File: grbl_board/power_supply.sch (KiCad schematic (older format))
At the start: 26 parts, among them J5 Screw_Terminal_01x04, U3 LT1962-5, U4 BD9G341EFJ

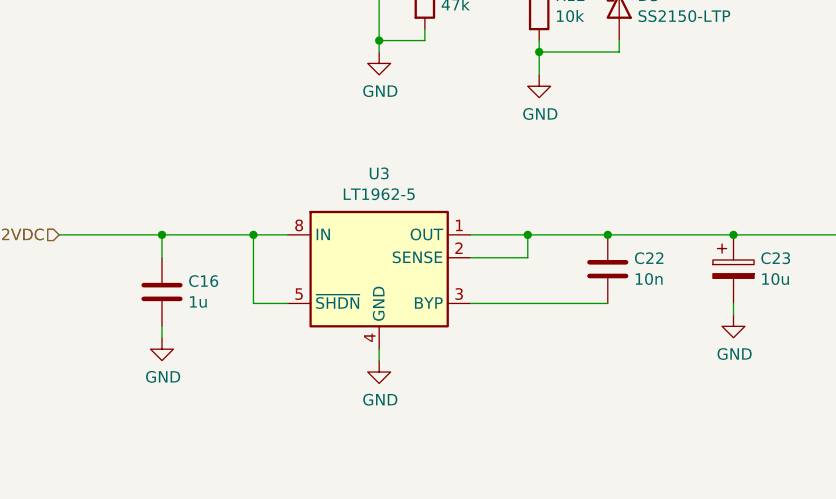
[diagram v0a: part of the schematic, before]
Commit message: fixed pullup resistors on board, and 5v regulator overheating, and stepper driver flipped
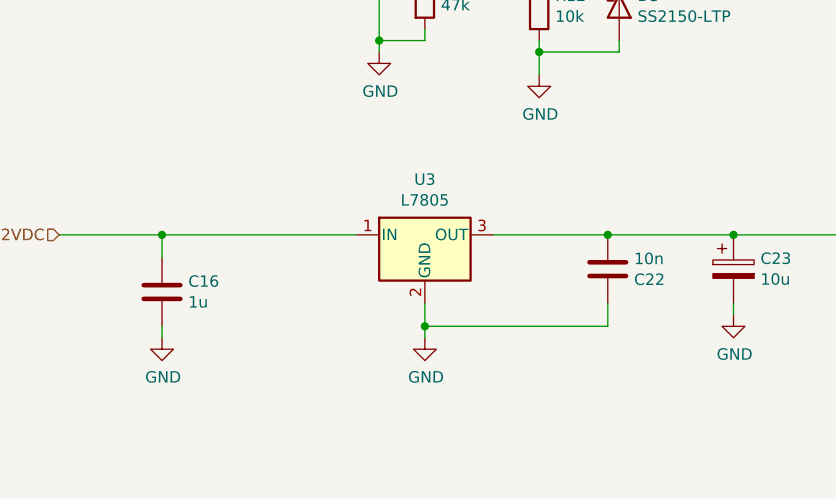
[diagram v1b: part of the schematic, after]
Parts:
- removed U3: LT1962-5, Package_SO:MSOP-8_3x3mm_P0.65mm, symbol Regulator_Linear:LT1962-5
- added U3: L7805, Package_TO_SOT_SMD:TO-263-2, symbol Regulator_Linear:L7805
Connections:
- net 12VDC: now also U3.1 (IN)
- net GND: now also C22.1, U3.2 (GND)
- net at C23.1, F2.2: now also C22.2, U3.3 (OUT); no longer C22.1
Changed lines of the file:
@@
 Text HLabel 7600 2800 2    50   Input ~ 0
 12VDC
-$Comp
-L Regulator_Linear:LT1962-5 U3
-U 1 1 617DD5A8
-P 5100 5050
-F 0 "U3" H 5100 5517 50  0000 C CNN
-F 1 "LT1962-5" H 5100 5426 50  0000 C CNN
-F 2 "Package_SO:MSOP-8_3x3mm_P0.65mm" H 5100 4700 50  0001 C CNN
-F 3 "https://www.analog.com/media/en/technical-documentation/data-sheets/1962fb.pdf" H 5100 4500 50  0001 C CNN
-F 4 "LT1962EMS8-5#TRPBFCT-ND" H 5100 5050 50  0001 C CNN "Digikey Part No."
-	1    5100 5050
-	1    0    0    -1
-$EndComp
 Text HLabel 3700 4850 0    50   Input ~ 0
 12VDC
 Wire Wire Line
 	3700 4850 4150 4850
-Wire Wire Line
-	4550 4850 4550 5150
-Wire Wire Line
-	4550 5150 4700 5150
-Connection ~ 4550 4850
-Wire Wire Line
-	4550 4850 4700 4850
 $Comp
 L Device:C C16
@@
 Wire Wire Line
 	4150 4950 4150 4850
-Connection ~ 4150 4850
-Wire Wire Line
-	4150 4850 4550 4850
 $Comp
 L power:GND #PWR022
@@
 	1    0    0    -1
 $EndComp
-$Comp
-L power:GND #PWR025
-U 1 1 617E1EFF
-P 5100 5400
-F 0 "#PWR025" H 5100 5150 50  0001 C CNN
-F 1 "GND" H 5105 5227 50  0000 C CNN
-F 2 "" H 5100 5400 50  0001 C CNN
-F 3 "" H 5100 5400 50  0001 C CNN
-	1    5100 5400
-	1    0    0    -1
-$EndComp
-Wire Wire Line
-	5100 5400 5100 5350
 Wire Wire Line
 	4150 5300 4150 5250
@@
 F 4 "1276-1009-1-ND" H 6100 5000 50  0001 C CNN "Digikey Part No."
 	1    6100 5000
-	1    0    0    -1
-$EndComp
-Wire Wire Line
-	6100 5150 5500 5150
-Wire Wire Line
-	6100 4850 5750 4850
-Wire Wire Line
-	5500 4950 5750 4950
-Wire Wire Line
-	5750 4950 5750 4850
-Connection ~ 5750 4850
-Wire Wire Line
-	5750 4850 5500 4850
+	1    0    0    1
+$EndComp
 $Comp
 L power:GND #PWR028
@@
 Wire Wire Line
 	6100 4850 6650 4850
-Connection ~ 6100 4850
 Connection ~ 6650 4850
 $Comp
@@
 	3800 1750 3700 1750
 Connection ~ 3800 1750
+$Comp
+L Regulator_Linear:L7805 U?
+U 1 1 61B77D83
+P 5300 4850
+AR Path="/61DA711F/61B77D83" Ref="U?"  Part="1"
+AR Path="/619755E7/61B77D83" Ref="U3"  Part="1"
+F 0 "U3" H 5300 5092 50  0000 C CNN
+F 1 "L7805" H 5300 5001 50  0000 C CNN
+F 2 "Package_TO_SOT_SMD:TO-263-2" H 5325 4700 50  0001 L CIN
+F 3 "http://www.st.com/content/ccc/resource/technical/document/datasheet/41/4f/b3/b0/12/d4/47/88/CD00000444.pdf/files/CD00000444.pdf/jcr:content/translations/en.CD00000444.pdf" H 5300 4800 50  0001 C CNN
+F 4 "497-1170-1-ND" H 5300 4850 50  0001 C CNN "Digikey Part No."
+	1    5300 4850
+	1    0    0    -1
+$EndComp
+Wire Wire Line
+	5600 4850 6100 4850
+Connection ~ 6100 4850
+Wire Wire Line
+	5000 4850 4150 4850
+Connection ~ 4150 4850
+$Comp
+L power:GND #PWR025
+U 1 1 61B84416
+P 5300 5300
+F 0 "#PWR025" H 5300 5050 50  0001 C CNN
+F 1 "GND" H 5305 5127 50  0000 C CNN
+F 2 "" H 5300 5300 50  0001 C CNN
+F 3 "" H 5300 5300 50  0001 C CNN
+	1    5300 5300
+	1    0    0    -1
+$EndComp
+Wire Wire Line
+	5300 5300 5300 5250
+Wire Wire Line
+	5300 5250 6100 5250
+Wire Wire Line
+	6100 5250 6100 5150
+Connection ~ 5300 5250
+Wire Wire Line
+	5300 5250 5300 5150
 $EndSCHEMATC

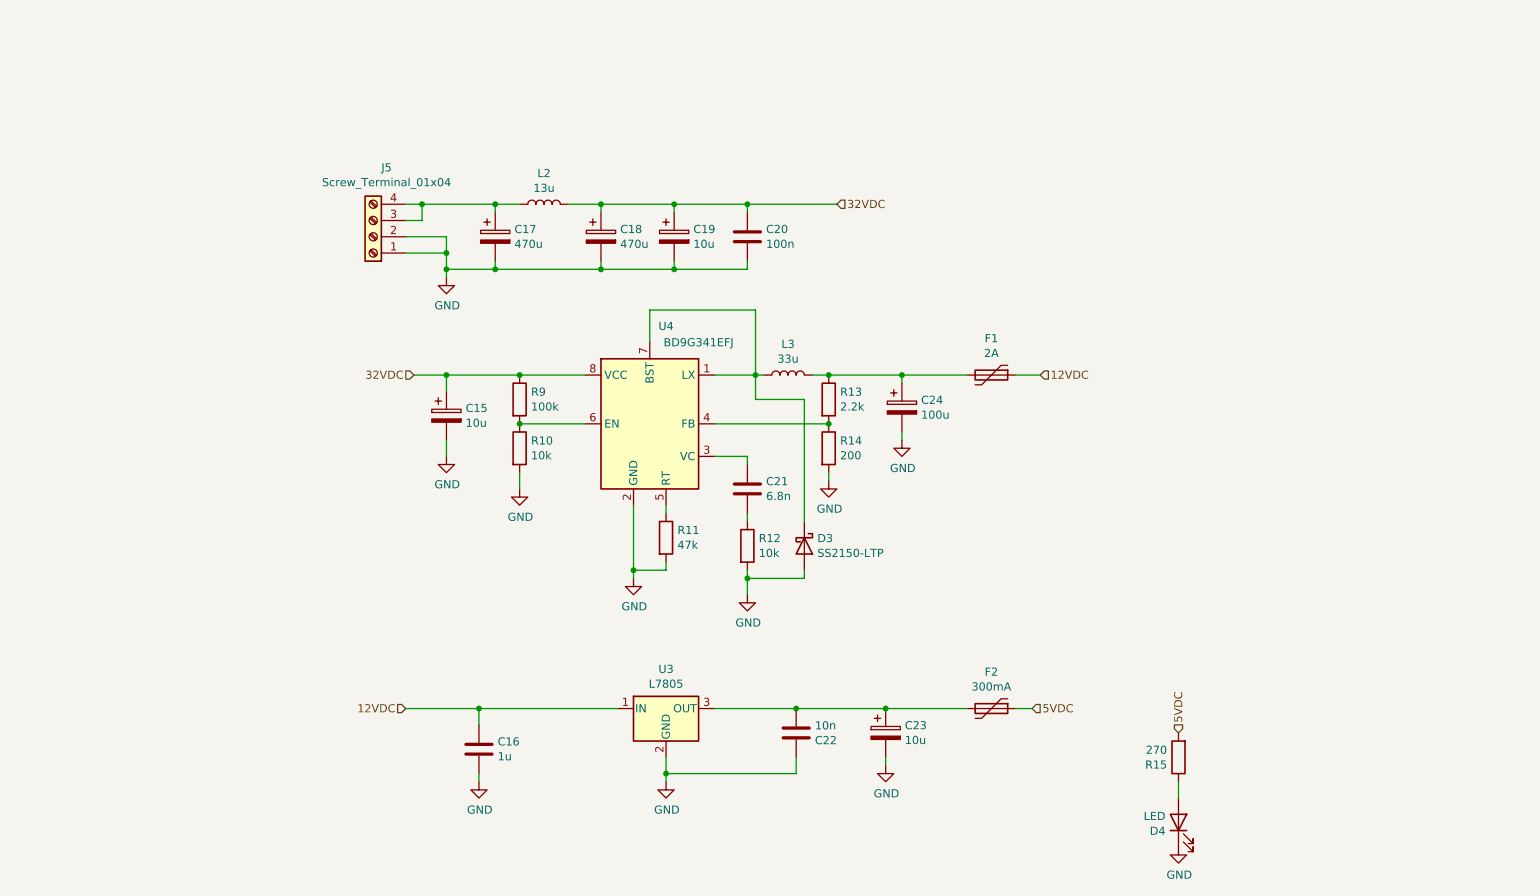
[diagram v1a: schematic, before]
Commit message: updated board with 24V reg
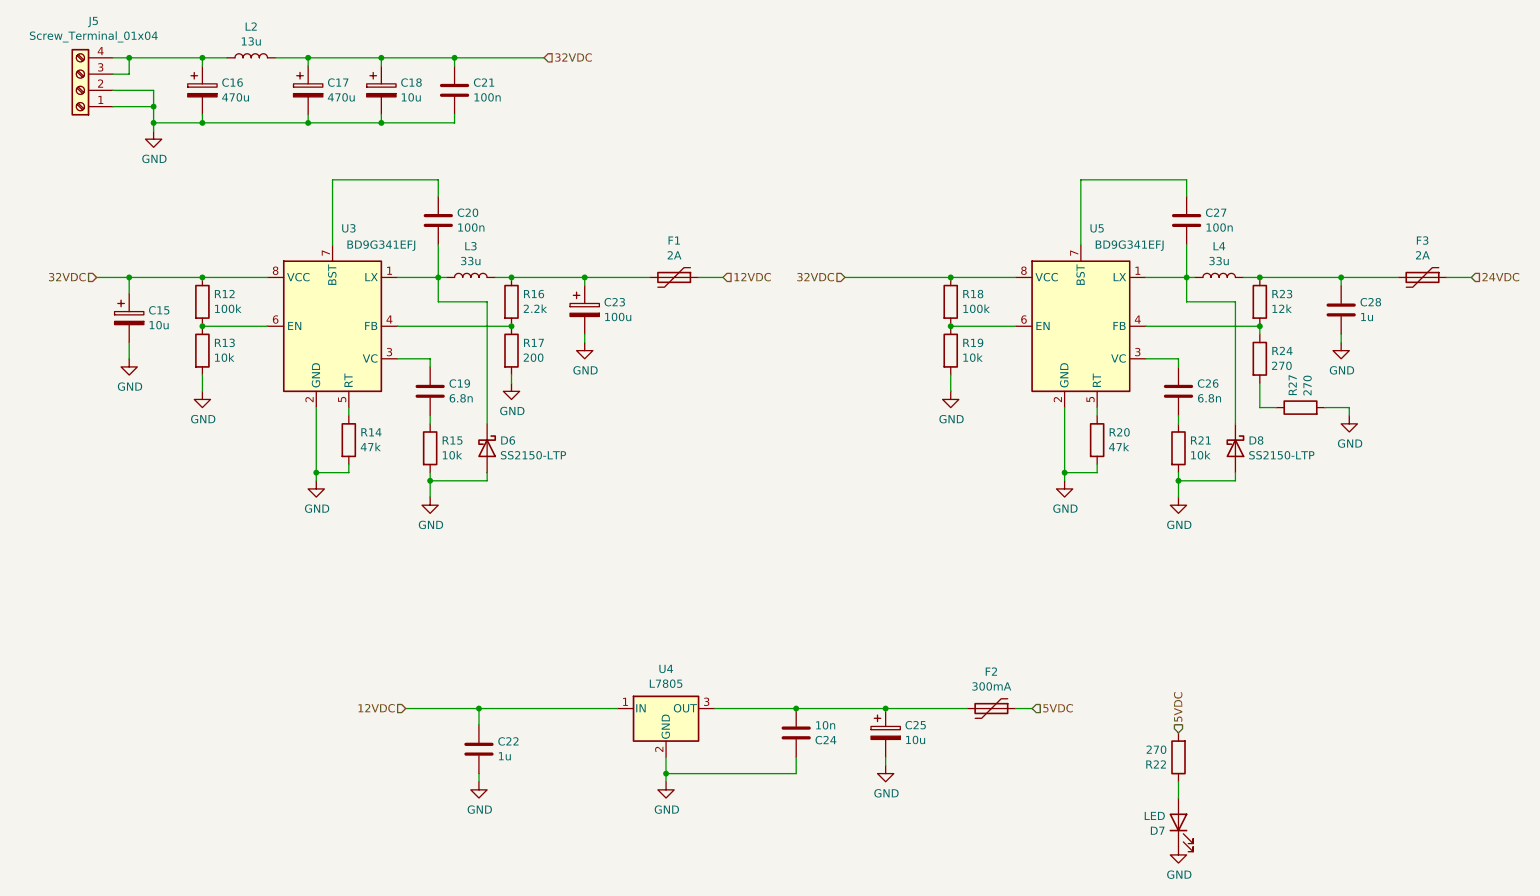
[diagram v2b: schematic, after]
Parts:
- added C20, C27: 100n, Capacitor_SMD:C_0603_1608Metric_Pad1.05x0.95mm_HandSolder, symbol Device:C
- added C26: 6.8n, Capacitor_SMD:C_0402_1005Metric_Pad0.74x0.62mm_HandSolder, symbol Device:C
- added C28: 1u, Capacitor_SMD:C_1206_3216Metric_Pad1.33x1.80mm_HandSolder, symbol Device:C
- added D8: SS2150-LTP, Diode_SMD:D_SMA_Handsoldering, symbol Device:D_Schottky
- added F3: 2A, Fuse:Fuse_Bourns_MF-RHT200, symbol Device:Polyfuse
- added L4: 33u, Inductor_SMD:L_Vishay_IHLP-4040, symbol Device:L
- added R18: 100k, Resistor_SMD:R_0603_1608Metric_Pad0.98x0.95mm_HandSolder, symbol Device:R
- added R19, R21: 10k, Resistor_SMD:R_0805_2012Metric_Pad1.15x1.40mm_HandSolder, symbol Device:R
- added R20: 47k, Resistor_SMD:R_0805_2012Metric_Pad1.15x1.40mm_HandSolder, symbol Device:R
- added R23: 12k, Resistor_SMD:R_0805_2012Metric_Pad1.15x1.40mm_HandSolder, symbol Device:R
- added R24, R27: 270, Resistor_SMD:R_0805_2012Metric_Pad1.15x1.40mm_HandSolder, symbol Device:R
- added U5: BD9G341EFJ, Package_SO:HTSOP-8-1EP_3.9x4.9mm_P1.27mm_EP2.4x3.2mm_ThermalVias, symbol Regulator_Switching:BD9G341EFJ
- renumbered C17 to C16, C18 to C17, C19 to C18, C21 to C19, C20 to C21, C16 to C22, C24 to C23, C22 to C24, C23 to C25, D3 to D6, D4 to D7, R9 to R12, R10 to R13, R11 to R14, R12 to R15, R13 to R16, R14 to R17, R15 to R22, U4 to U3, U3 to U4
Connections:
- net 32VDC: now also R18.1, U5.8 (VCC)
- net GND: now also C28.2, D8.2 (A), R19.2, R20.2, R21.2, R27.2, U5.2 (GND)
- net at D6.1 (K), L3.1, U3.1 (LX): now also C20.2; no longer U3.7 (BST)
- new net: C20.1, U3.7 (BST)
- new net: C27.2, D8.1 (K), L4.1, U5.1 (LX)
- new net: C26.1, U5.3 (VC)
- new net: R23.2, R24.1, U5.4 (FB)
- new net: R20.1, U5.5 (RT)
- new net: R18.2, R19.1, U5.6 (EN)
- new net: C27.1, U5.7 (BST)
- new net: C26.2, R21.1
- new net: C28.1, F3.2, L4.2, R23.1
- new net: R24.2, R27.1
- new net 24VDC: F3.1
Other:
- moved on the sheet: C15, C16, C17, C18, C19, C21, C23, D6, F1, J5, L2, L3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
